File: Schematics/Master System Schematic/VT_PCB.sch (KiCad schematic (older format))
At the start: 34 parts, among them K18 Voltage Tap Relay, K19 Voltage Tap Relay, K20 Voltage Tap Relay, K21 Voltage Tap Relay, K22 Voltage Tap Relay

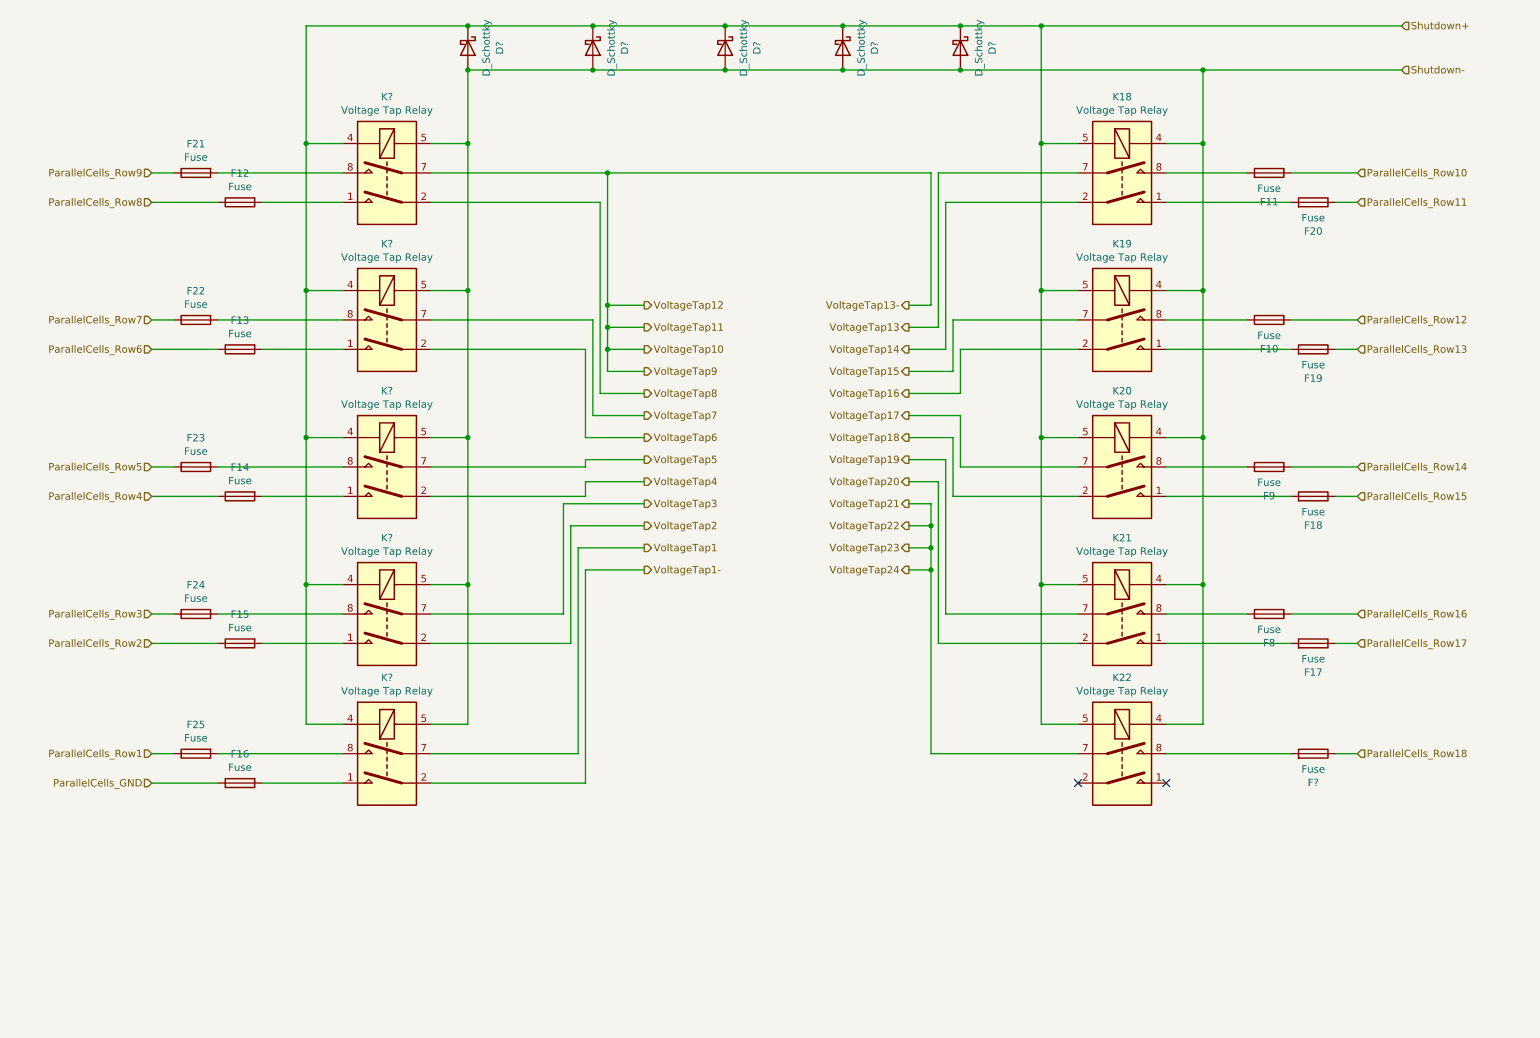
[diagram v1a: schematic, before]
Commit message: cleanup on VT pcbs
>made vt relay boards much cleaner
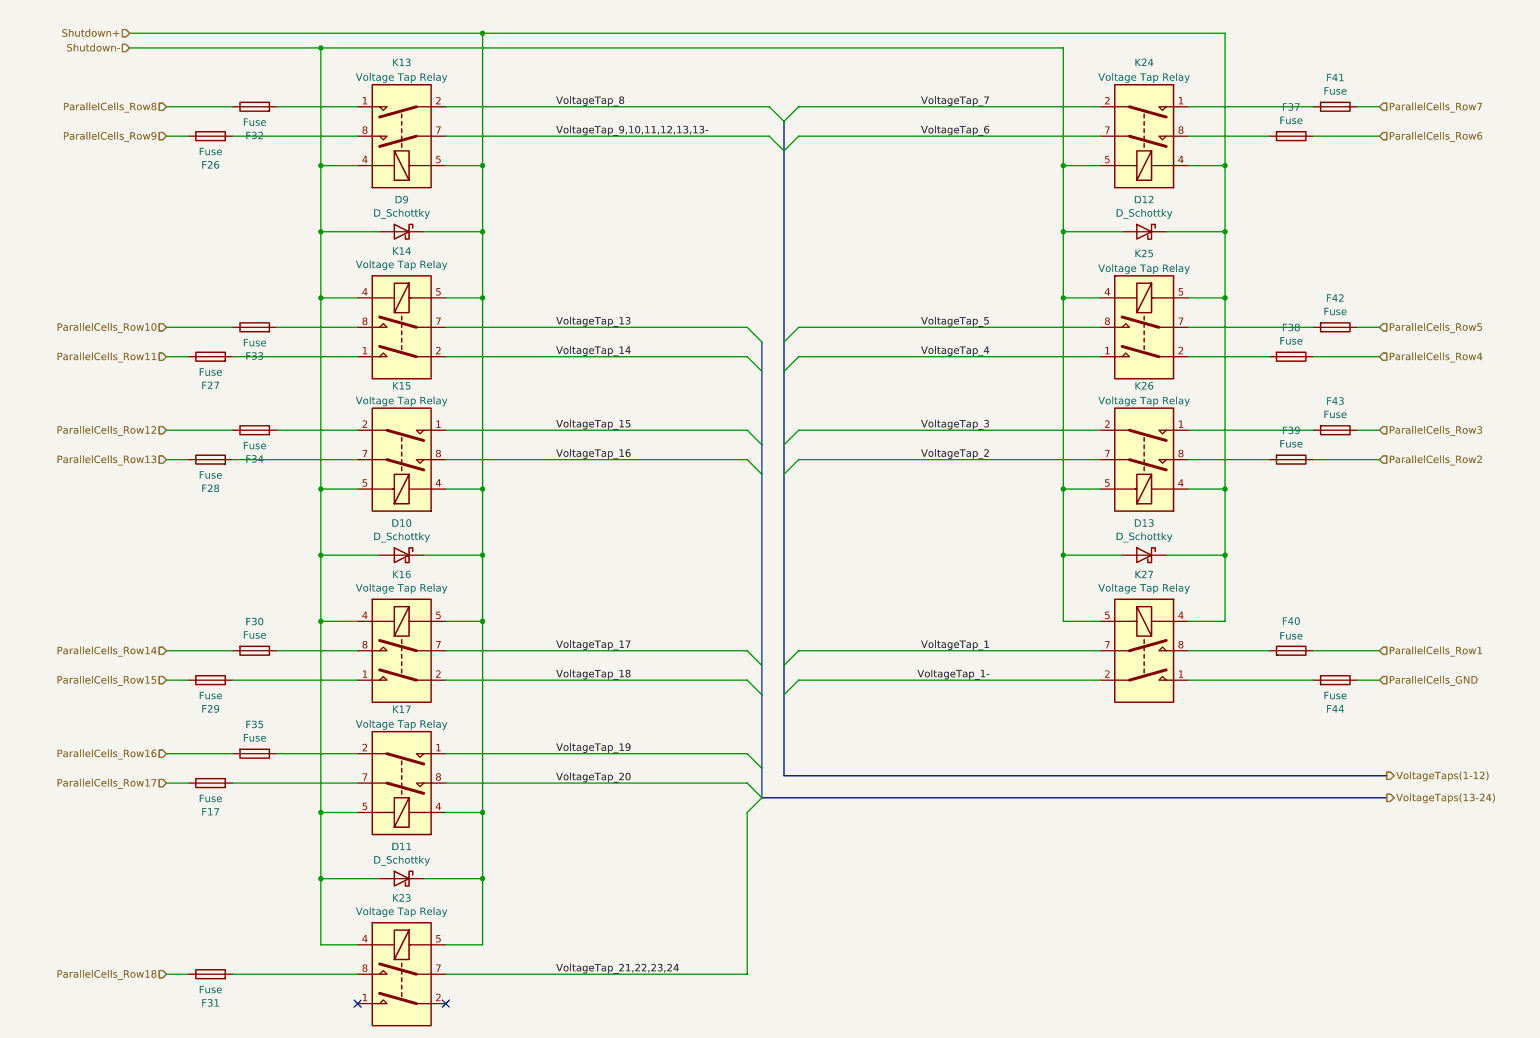
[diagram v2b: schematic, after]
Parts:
- removed F17, F8, F9: Fuse, symbol Device:Fuse
- added F36, F50, F55: Fuse, symbol Device:Fuse
- gave numbers to parts that had none: 11
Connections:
- net VoltageTap15 is gone; now on an unnamed net: K19.7
- net VoltageTap16 is gone; now on an unnamed net: K19.2
- net VoltageTap4 is gone; now on an unnamed net: K30.2
- net VoltageTap5 is gone; now on an unnamed net: K30.7
- net ParallelCells_GND: now also F25.1; no longer F16.1
- net ParallelCells_Row1: now also F16.1; no longer F25.1
- net ParallelCells_Row14: now also F50.2
- net ParallelCells_Row16: now also F55.2
- net ParallelCells_Row17: now also F36.1
- net Shutdown+: now also K19.4, K21.4, K28.5, K30.5; no longer K19.5, K21.5, K28.4, K30.4
- net Shutdown-: now also K19.5, K21.5, K28.4, K30.4; no longer K19.4, K21.4, K28.5, K30.5
- net at K29.1: now also F22.2; no longer F13.2
- net at K29.8: now also F13.2; no longer F22.2
- net at F14.2: no longer K30.1
- net at F23.2: no longer K30.8
- net at K32.1: now also F25.2; no longer F15.2
- net at K32.8: now also F16.2; no longer F24.2
- net at K31.1: now also F24.2; no longer F16.2
- net at K31.8: now also F15.2; no longer F25.2
- net at F19.2: no longer K19.1
- net at F10.2: no longer K19.8
- net at K20.8: now also F50.1
- net VoltageTap_19: now reaches K21.1
- net VoltageTap_20: now reaches K21.8
- net VoltageTap1 renamed VoltageTap_2
- net VoltageTap1- renamed VoltageTap_3
- net VoltageTap10 renamed VoltageTap_9,10,11,12,13,13-
- net VoltageTap13 renamed VoltageTap_13
- net VoltageTap14 renamed VoltageTap_14
- net VoltageTap17 renamed VoltageTap_17
- net VoltageTap18 renamed VoltageTap_18
- net VoltageTap19: no longer names the net of K21.7
- net VoltageTap19: now also F36.2
- net VoltageTap2 renamed VoltageTap_1-
- net VoltageTap20: no longer names the net of K21.2
- net VoltageTap20: now also F55.1
- net VoltageTap21 renamed VoltageTap_21,22,23,24
- net VoltageTap3 renamed VoltageTap_1
- net VoltageTap6 renamed VoltageTap_7
- net VoltageTap7 renamed VoltageTap_6
- net VoltageTap8 renamed VoltageTap_8
- new net VoltageTap_15: K19.1
- new net VoltageTap_16: K19.8
- new net VoltageTap_4: K30.1
- new net VoltageTap_5: K30.8
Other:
- moved on the sheet: D10, D11, D12, D13, D9, F26, F27, F28, F29, F31, F32, F33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

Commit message: FINISHED Voltage tap PCB schem
>reran battery box to fit new schem
>added placeholder thermistor board schem.
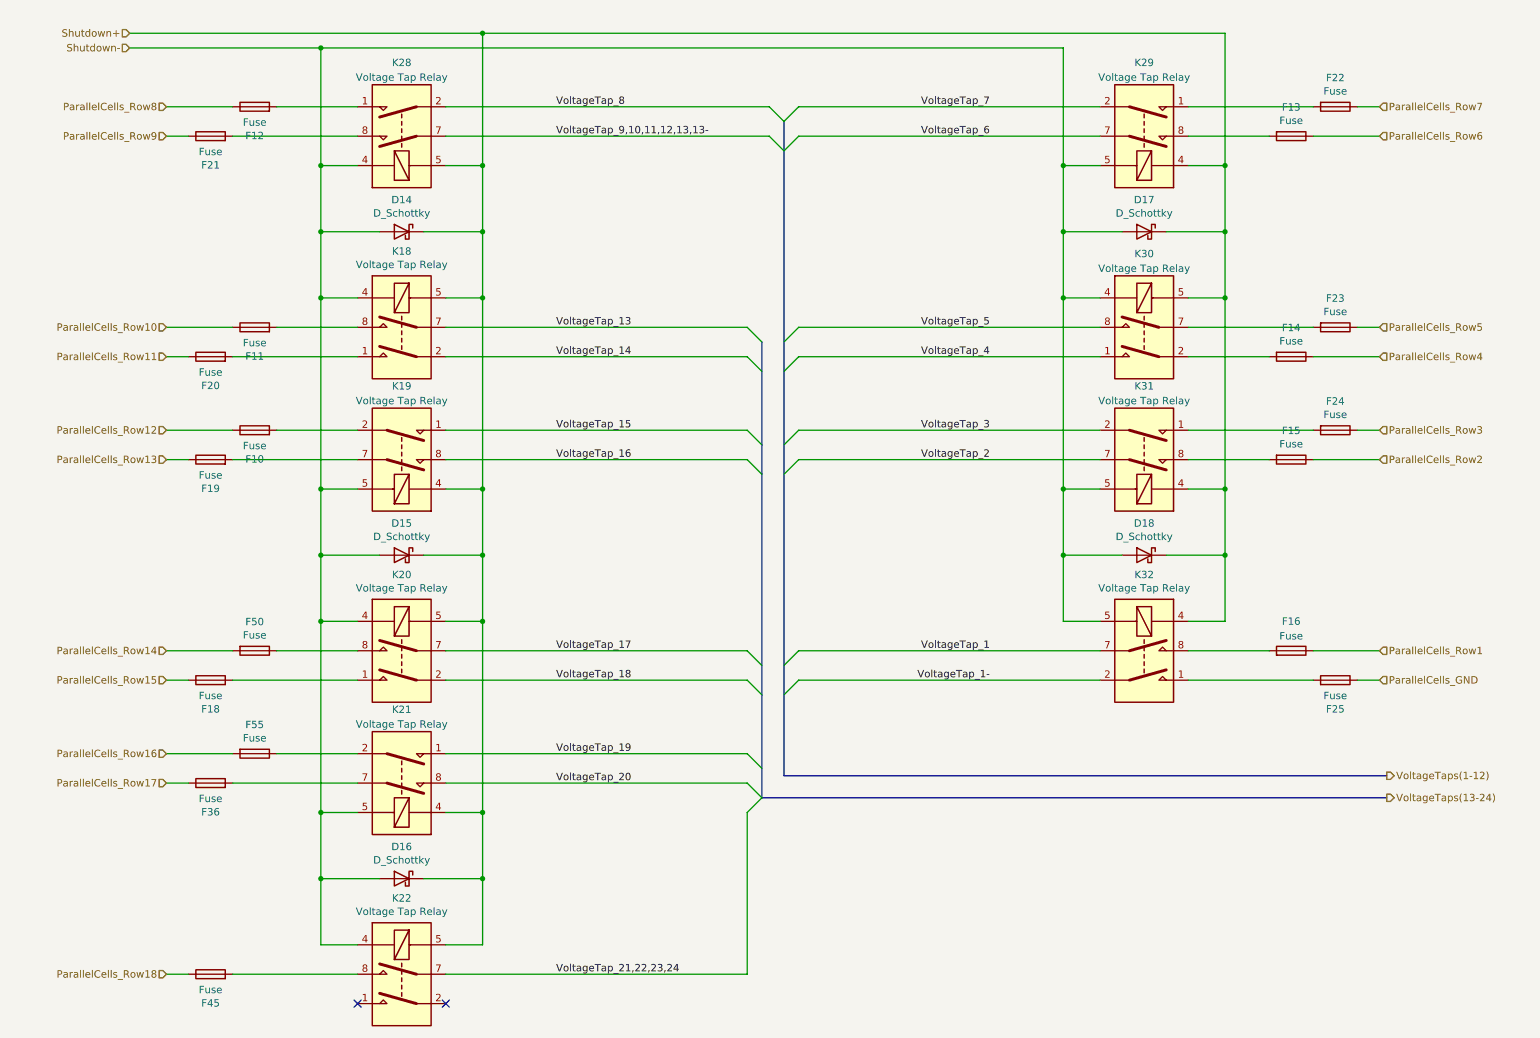
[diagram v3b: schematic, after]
